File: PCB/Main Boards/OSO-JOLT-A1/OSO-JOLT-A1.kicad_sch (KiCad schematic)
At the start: 35 parts, among them J1 OSO_SWD, J2 FH19C-9S-0.5SH_10_, Q1 Q_Photo_NPN, Q2 Q_NMOS_GSD, U1 ATSAML22J18A-MUT, U2 MIC5365-3.3YC5-TR, X1 Crystal

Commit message: Began routing
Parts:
- removed D2: QBLP655-RGB, OSO-SWAT-A1-05:LED_QBLP655_RGB, symbol OSO-SWAT-A1-05-eagle-import:QBLP655-RGB
- removed Q1: Q_Photo_NPN, Resistor_SMD:R_0603_1608Metric, symbol Device:Q_Photo_NPN
- removed R1: 10K, Resistor_SMD:R_0201_0603Metric, symbol OSO-SWAT-A1-05-eagle-import:RESISTOR_0603MP
- removed R6: 1K, Resistor_SMD:R_0603_1608Metric, symbol OSO-SWAT-A1-05-eagle-import:RESISTOR_0603MP
- removed R7: 100, Resistor_SMD:R_0603_1608Metric, symbol OSO-SWAT-A1-05-eagle-import:RESISTOR_0603MP
- removed U$2: SENSOR-WATCH-USB, OSO-SWAT-A1-05:CASIO-F91W-OUTLINE-USB, symbol OSO-SWAT-A1-05-eagle-import:SENSOR-WATCH-USB
- added D2: QBLP617-IW, OSO-SWAT-A1-05:LED_QBLP617, symbol OSO-SWAT-A1-05-eagle-import:QBLP617-IW
- added TP11: MICROBUILDER_TESTPOINTROUND1.5MM, OSO-SWAT-A1-05:MICROBUILDER_TESTPOINT_ROUND_1.5MM, symbol OSO-SWAT-A1-05-eagle-import:MICROBUILDER_TESTPOINTROUND1.5MM
- added U3: SENSOR-WATCH-JOLT-USB, OSO-SWAT-A1-05:CASIO-DW5600-OUTLINE-USB, symbol OSO-SWD:SENSOR-WATCH-JOLT-USB
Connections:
- net BUZZER_HV: now also U3.BUZZER1, U3.BUZZER2
- net COM0: now also U3.A16
- net COM1: now also U3.A17
- net COM2: now also U3.A18
- net GND: now also U3.GND, U3.GND1, U3.GND2, U3.GND3, U3.SINK1, U3.SINK2, U3.SINK3, U3.SINK4
- net SEG0: now also U3.A15
- net SEG1: now also U3.A14
- net SEG10: now also U3.A5
- net SEG11: now also U3.B18
- net SEG12: now also U3.B17
- net SEG13: now also U3.B16
- net SEG14: now also U3.B15
- net SEG15: now also U3.B13
- net SEG16: now also U3.B13
- net SEG17: now also U3.B12
- net SEG18: now also U3.B11
- net SEG19: now also U3.B10
- net SEG2: now also U3.A13
- net SEG20: now also U3.B9
- net SEG21: now also U3.B8
- net SEG22: now also U3.B7
- net SEG23: now also U3.B6
- net SEG3: now also U3.A12
- net SEG4: now also U3.A11
- net SEG5: now also U3.A10
- net SEG6: now also U3.A9
- net SEG7: now also U3.A8
- net SEG8: now also U3.A7
- net SEG9: now also U3.A6
- net SWCLK_LIGHT: now also TP11.P$1, U3.LIGHT; no longer TP8.P$1
- net SWDIO_MODE: now also U3.MODE
- net USB_N: now also U3.USB_N (D-)
- net USB_P: now also U3.USB_P (D+)
- net VBUS: now also U3.VBUS
- net VCC: now also D2.1 (A), U3.VCC1
- net at R8.2: now also D2.2 (C)
- net A0: no longer names the net of J2.9
- net A0: no longer U1.5 (PB04/I4/AIN12)
- net ALARM renamed ADJUST
- net ADJUST: now also TP8.P$1, U3.ALARM (ADJUST); no longer TP10.P$1
- net LIGHTSENSE renamed COM3
- net COM3: now also U3.A19
- net ~{BLUE} renamed SEG25
- net SEG25: now also U3.B4; no longer R8.1
- net ~{GREEN} renamed SEG26
- net SEG26: now also U3.B3
- net ~{LS_ENABLE} renamed ~{LED}
- net ~{LED}: now also R8.1
- net ~{RED} renamed SEG24
- net SEG24: now also U3.B5
- new net START: TP10.P$1, U1.5 (PB04/I4/AIN12), U3.START
- no-connect marks 1 -> 8

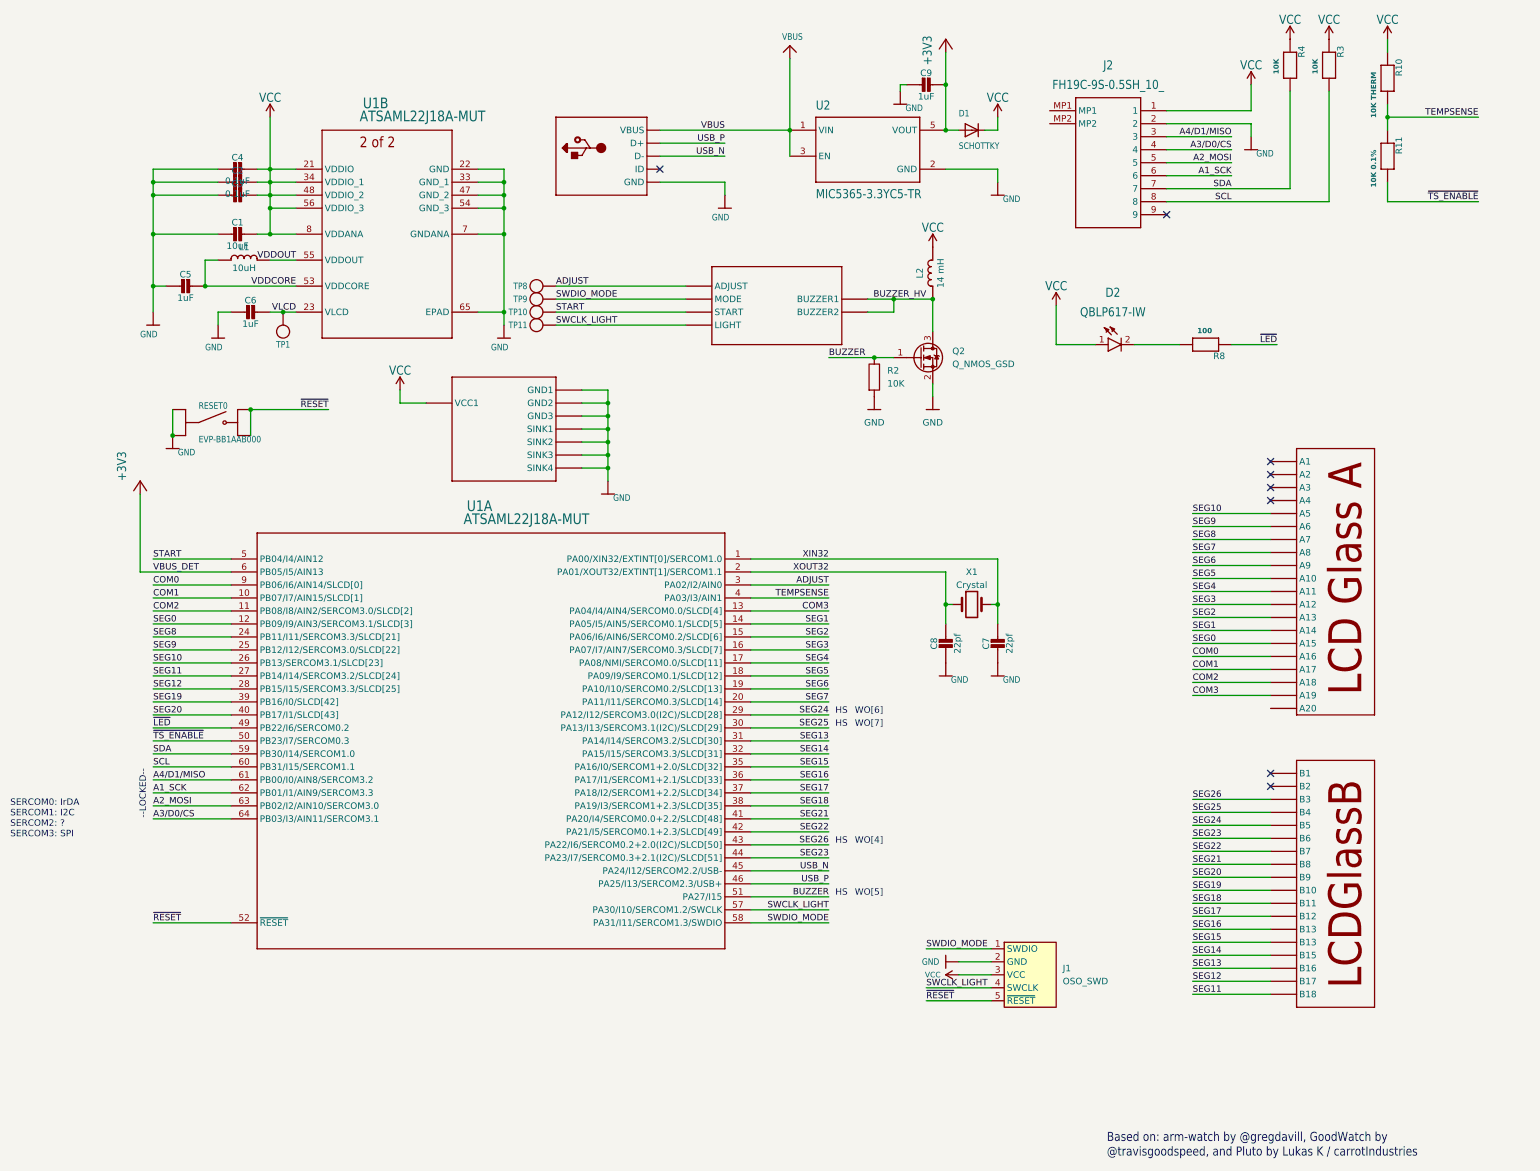
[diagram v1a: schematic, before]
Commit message: Began routing and added courtyard for light bracket
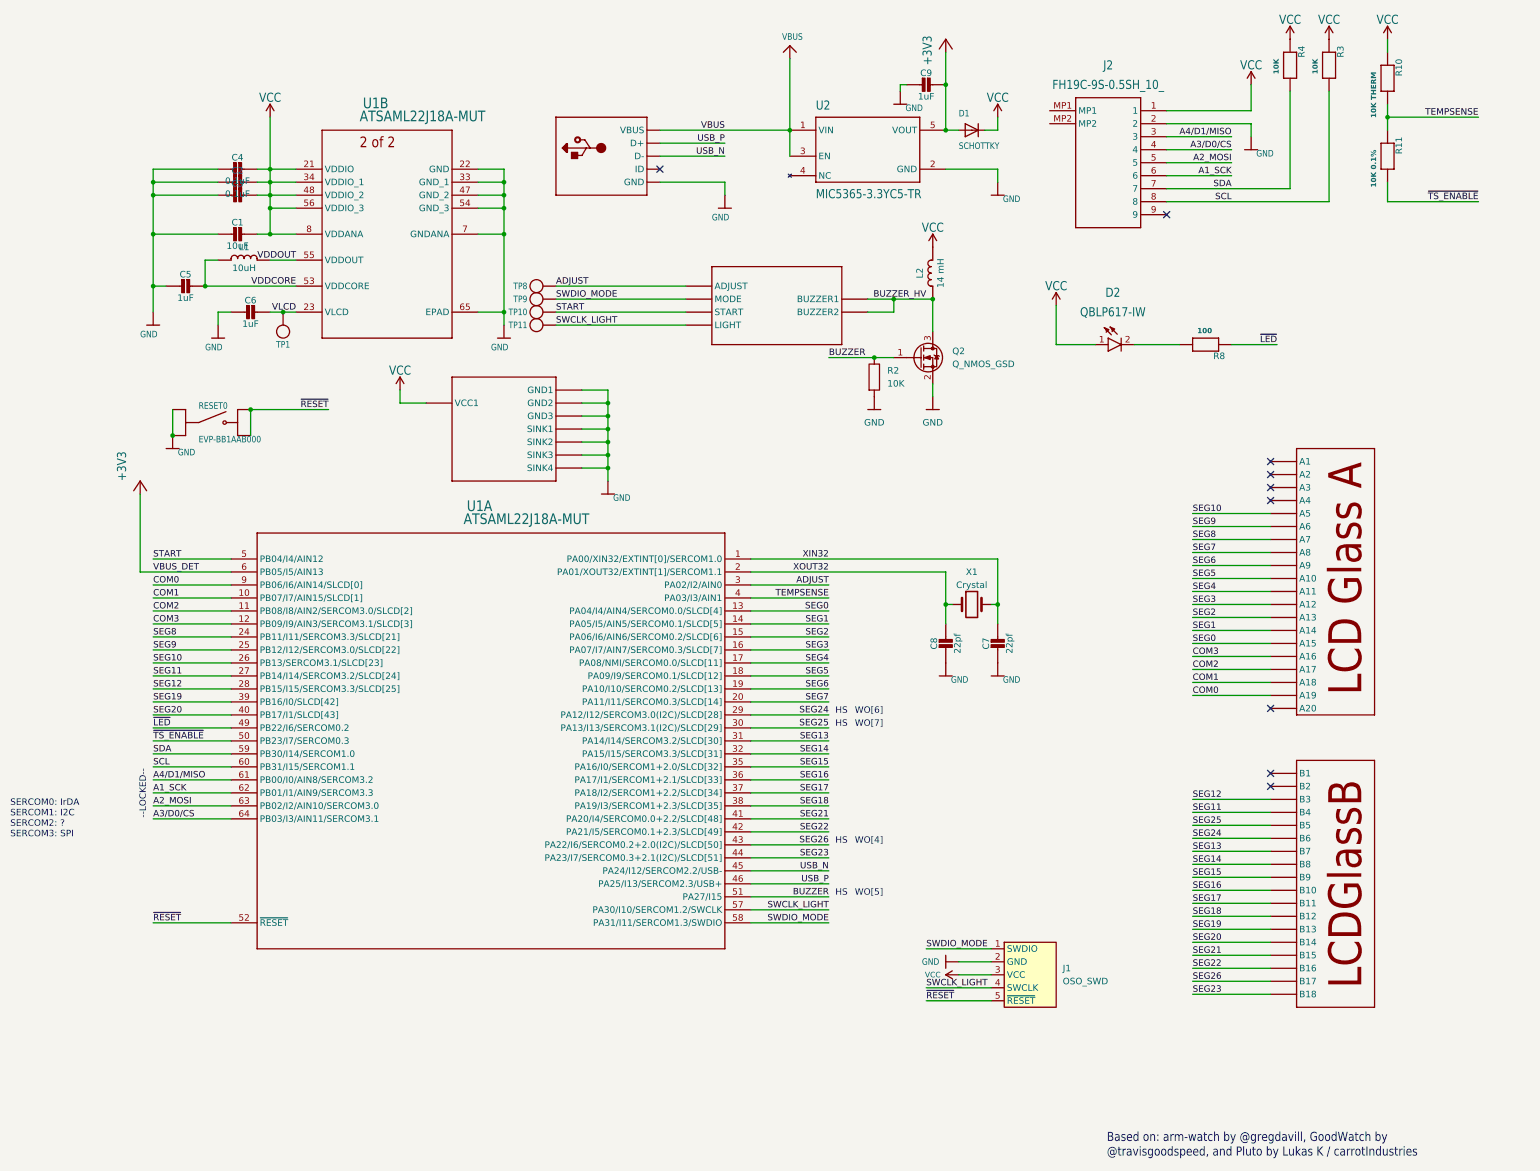
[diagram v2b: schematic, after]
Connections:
- net ADJUST: now also U3.ADJUST; no longer U3.ALARM (ADJUST)
- net COM0: now also U3.A19; no longer U3.A16
- net COM1: now also U3.A18; no longer U3.A17
- net COM2: now also U3.A17; no longer U3.A18
- net COM3: now also U1.12 (PB09/I9/AIN3/SERCOM3.1/SLCD[3]), U3.A16; no longer U1.13 (PA04/I4/AIN4/SERCOM0.0/SLCD[4]), U3.A19
- net SEG0: now also U1.13 (PA04/I4/AIN4/SERCOM0.0/SLCD[4]); no longer U1.12 (PB09/I9/AIN3/SERCOM3.1/SLCD[3])
- net SEG11: now also U3.B4; no longer U3.B18
- net SEG12: now also U3.B3; no longer U3.B17
- net SEG13: now also U3.B7; no longer U3.B16
- net SEG14: now also U3.B8; no longer U3.B15
- net SEG15: now also U3.B9; no longer U3.B13
- net SEG16: now also U3.B10; no longer U3.B13
- net SEG17: now also U3.B11; no longer U3.B12
- net SEG18: now also U3.B12; no longer U3.B11
- net SEG19: now also U3.B13; no longer U3.B10
- net SEG20: now also U3.B14; no longer U3.B9
- net SEG21: now also U3.B15; no longer U3.B8
- net SEG22: now also U3.B16; no longer U3.B7
- net SEG23: now also U3.B18; no longer U3.B6
- net SEG24: now also U3.B6; no longer U3.B5
- net SEG25: now also U3.B5; no longer U3.B4
- net SEG26: now also U3.B17; no longer U3.B3
- no-connect marks 8 -> 9

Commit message: Seperate DW5600 components and made the edge cuts live on thepcb
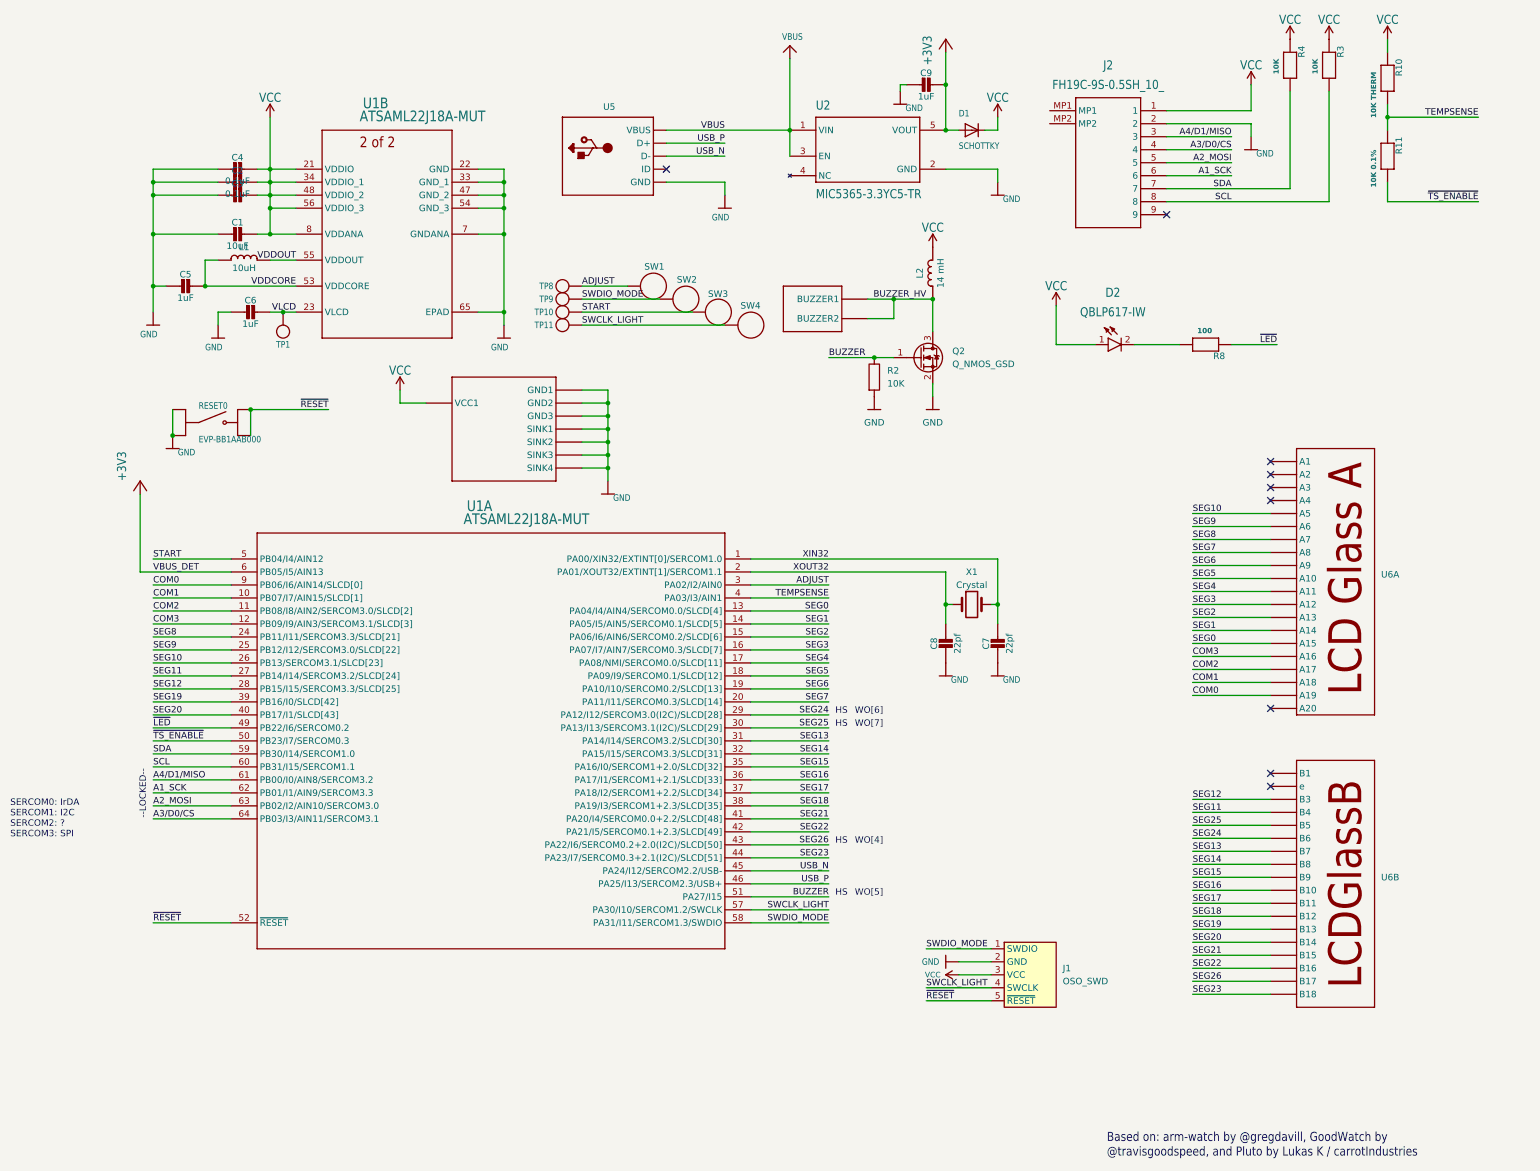
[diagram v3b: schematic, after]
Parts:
- removed U3: SENSOR-WATCH-JOLT-USB, OSO-SWAT-A1-05:CASIO-DW5600-OUTLINE-USB, symbol OSO-SWD:SENSOR-WATCH-JOLT-USB
- added SW1, SW3: (no value), OSO-SWAT-A1-05:CASIO-DW5600-BTN, symbol OSO-SWD:DW5600-BTN
- added SW2, SW4: ~, OSO-SWAT-A1-05:CASIO-DW5600-BTN, symbol OSO-SWD:DW5600-BTN
- added U4: ~, OSO-SWAT-A1-05:CASIO-DW5600-PWR-BUZZER, symbol OSO-SWD:DW5600-PWR
- added U5: ~, OSO-SWAT-A1-05:CASIO-DW5600-USB, symbol OSO-SWD:DW5600-USB
- added U6: ~, OSO-SWAT-A1-05:CASIO-DW5600-LCD, symbol OSO-SWD:DW5600-LCD
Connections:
- net ADJUST: now also SW1.BTN
- net BUZZER_HV: now also U4.BUZZER1, U4.BUZZER2
- net COM0: now also U6.A19
- net COM1: now also U6.A18
- net COM2: now also U6.A17
- net COM3: now also U6.A16
- net GND: now also U4.GND1, U4.GND2, U4.GND3, U4.SINK1, U4.SINK2, U4.SINK3, U4.SINK4, U5.GND
- net SEG0: now also U6.A15
- net SEG1: now also U6.A14
- net SEG10: now also U6.A5
- net SEG11: now also U6.B4
- net SEG12: now also U6.B3
- net SEG13: now also U6.B7
- net SEG14: now also U6.B8
- net SEG15: now also U6.B9
- net SEG16: now also U6.B10
- net SEG17: now also U6.B11
- net SEG18: now also U6.B12
- net SEG19: now also U6.B13
- net SEG2: now also U6.A13
- net SEG20: now also U6.B14
- net SEG21: now also U6.B15
- net SEG22: now also U6.B16
- net SEG23: now also U6.B18
- net SEG24: now also U6.B6
- net SEG25: now also U6.B5
- net SEG26: now also U6.B17
- net SEG3: now also U6.A12
- net SEG4: now also U6.A11
- net SEG5: now also U6.A10
- net SEG6: now also U6.A9
- net SEG7: now also U6.A8
- net SEG8: now also U6.A7
- net SEG9: now also U6.A6
- net START: now also SW3.BTN
- net SWCLK_LIGHT: now also SW4.BTN
- net SWDIO_MODE: now also SW2.BTN
- net USB_N: now also U5.USB_N (D-)
- net USB_P: now also U5.USB_P (D+)
- net VBUS: now also U5.VBUS
- net VCC: now also U4.VCC1
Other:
- moved on the sheet: TP10, TP11, TP8, TP9

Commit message: Resynced pcb and sch
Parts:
- SW1, SW3: value (none) -> ~
- renumbered C5 to C1, C4 to C2, C2 to C3, C3 to C4, C1 to C5, C9 to C7, C7 to C9, Q2 to Q1, R2 to R1, R8 to R2, R4 to R3, R3 to R4, R10 to R5, R11 to R6, RESET0 to RESET1, TP8 to TP2, TP9 to TP3, TP10 to TP4, TP11 to TP5, U4 to U2, U5 to U3, U2 to U4, U6 to U5
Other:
- moved on the sheet: C2, C3, C5, SW1, SW2, SW3, SW4, TP2, TP3, TP5

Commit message: end of day routing commit
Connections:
- net SEG11: now also U5.B17; no longer U5.B4
- net SEG12: now also U5.B18; no longer U5.B3
- net SEG13: now also U5.B14; no longer U5.B7
- net SEG14: now also U5.B13; no longer U5.B8
- net SEG15: now also U5.B12; no longer U5.B9
- net SEG16: now also U5.B11; no longer U5.B10
- net SEG17: now also U5.B3; no longer U5.B11
- net SEG18: now also U5.B4; no longer U5.B12
- net SEG19: now also U5.B5; no longer U5.B13
- net SEG20: now also U5.B6; no longer U5.B14
- net SEG21: now also U5.B7; no longer U5.B15
- net SEG22: now also U5.B8; no longer U5.B16
- net SEG23: now also U5.B10; no longer U5.B18
- net SEG24: now also U5.B15; no longer U5.B6
- net SEG25: now also U5.B16; no longer U5.B5
- net SEG26: now also U5.B9; no longer U5.B17

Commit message: Added all footprints
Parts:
- removed Q1: Q_NMOS_GSD, Package_TO_SOT_SMD:SOT-523, symbol Device:Q_NMOS_GSD
- removed TP2, TP3, TP4, TP5: MICROBUILDER_TESTPOINTROUND1.5MM, OSO-SWAT-A1-05:MICROBUILDER_TESTPOINT_ROUND_1.5MM, symbol OSO-SWAT-A1-05-eagle-import:MICROBUILDER_TESTPOINTROUND1.5MM
- added Q1: Q_NMOS_GSD, OSO-SWAT-A1-05:SOT-523, symbol OSO-SWD:Q_NMOS_GSD
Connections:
- net BUZZER: now also Q1.1 (G)
- net BUZZER_HV: now also Q1.3 (D)
- net GND: now also Q1.2 (S)
- net SEG11: now also U5.B18; no longer U5.B17
- net SEG12: now also U5.B17; no longer U5.B18
- net SEG24: now also U5.B16; no longer U5.B15
- net SEG25: now also U5.B15; no longer U5.B16

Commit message: Made back components larger in case I want to hand-solder them
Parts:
- C1: footprint Capacitor_SMD:C_0603_1608Metric -> Capacitor_SMD:C_0805_2012Metric; symbol OSO-SWAT-A1-05-eagle-import:CAP_CERAMIC_0603MP -> OSO-SWAT-A1-05-eagle-import:CAP_CERAMIC_0805
- R2: footprint Resistor_SMD:R_0603_1608Metric -> Resistor_SMD:R_0805_2012Metric
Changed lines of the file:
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@@
 			)
 		)
-		(property "Footprint" "Resistor_SMD:R_0603_1608Metric"
+		(property "Footprint" "Resistor_SMD:R_0805_2012Metric"
 			(at 236.22 72.39 0)
 			(effects
@@
 	)
 	(symbol
-		(lib_id "OSO-SWAT-A1-05-eagle-import:CAP_CERAMIC_0603MP")
+		(lib_id "OSO-SWAT-A1-05-eagle-import:CAP_CERAMIC_0805")
 		(at 35.56 60.96 270)
 		(unit 1)
@@
 			)
 		)
-		(property "Footprint" "Capacitor_SMD:C_0603_1608Metric"
+		(property "Footprint" "Capacitor_SMD:C_0805_2012Metric"
 			(at 35.56 60.96 0)
 			(effects

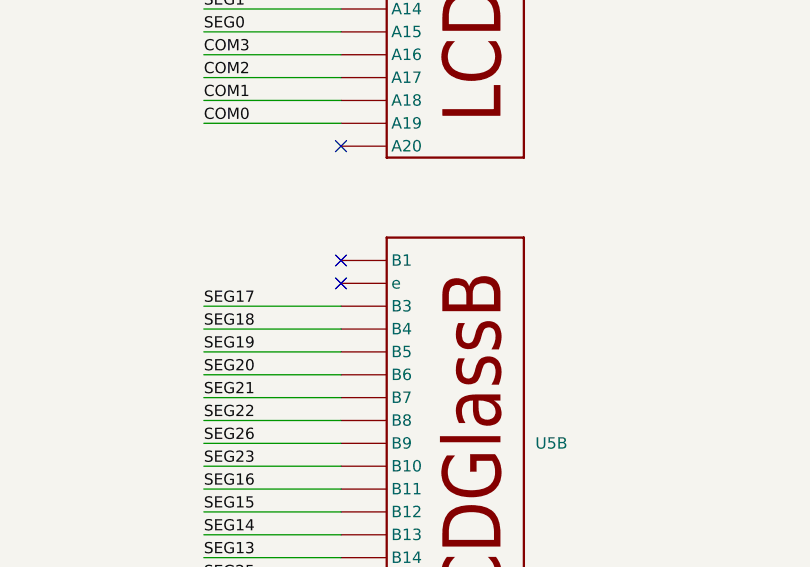
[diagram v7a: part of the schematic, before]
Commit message: Modified NMOS to match the one on the Pro
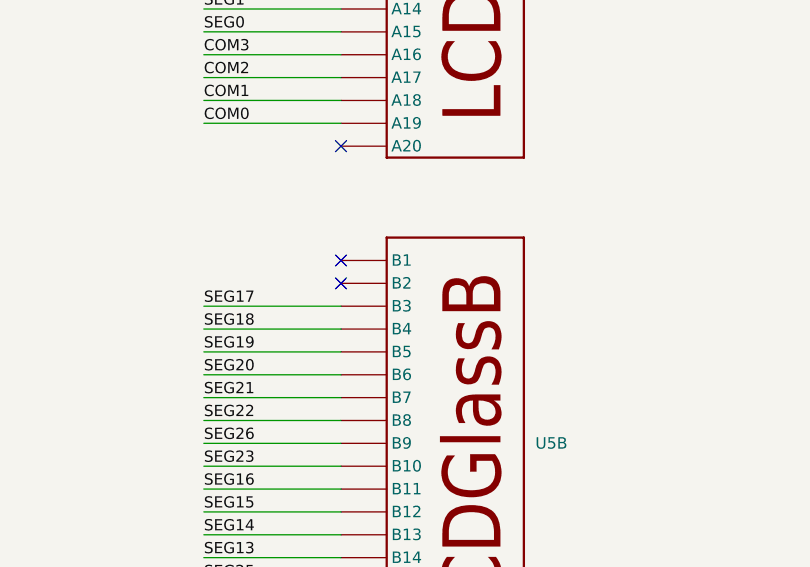
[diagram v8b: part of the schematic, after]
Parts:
- SW1, SW2, SW3, SW4, U2, U3, U5: now left out of the parts list
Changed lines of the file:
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@@
 		(unit 1)
 		(exclude_from_sim no)
-		(in_bom yes)
+		(in_bom no)
 		(on_board yes)
 		(dnp no)
@@
 		(unit 2)
 		(exclude_from_sim no)
-		(in_bom yes)
+		(in_bom no)
 		(on_board yes)
 		(dnp no)
@@
 		(unit 1)
 		(exclude_from_sim no)
-		(in_bom yes)
+		(in_bom no)
 		(on_board yes)
 		(dnp no)
@@
 		(unit 1)
 		(exclude_from_sim no)
-		(in_bom yes)
+		(in_bom no)
 		(on_board yes)
 		(dnp no)
@@
 		(unit 1)
 		(exclude_from_sim no)
-		(in_bom yes)
+		(in_bom no)
 		(on_board yes)
 		(dnp no)
@@
 		(unit 1)
 		(exclude_from_sim no)
-		(in_bom yes)
+		(in_bom no)
 		(on_board yes)
 		(dnp no)
@@
 		(unit 1)
 		(exclude_from_sim no)
-		(in_bom yes)
+		(in_bom no)
 		(on_board yes)
 		(dnp no)
@@
 		(unit 1)
 		(exclude_from_sim no)
-		(in_bom yes)
+		(in_bom no)
 		(on_board yes)
 		(dnp no)
@@
 		(unit 2)
 		(exclude_from_sim no)
-		(in_bom yes)
+		(in_bom no)
 		(on_board yes)
 		(dnp no)
